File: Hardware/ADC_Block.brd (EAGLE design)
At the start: 30.5 x 44.5 mm, 28 parts, among them U1 ADS1015, U2 PCA9306

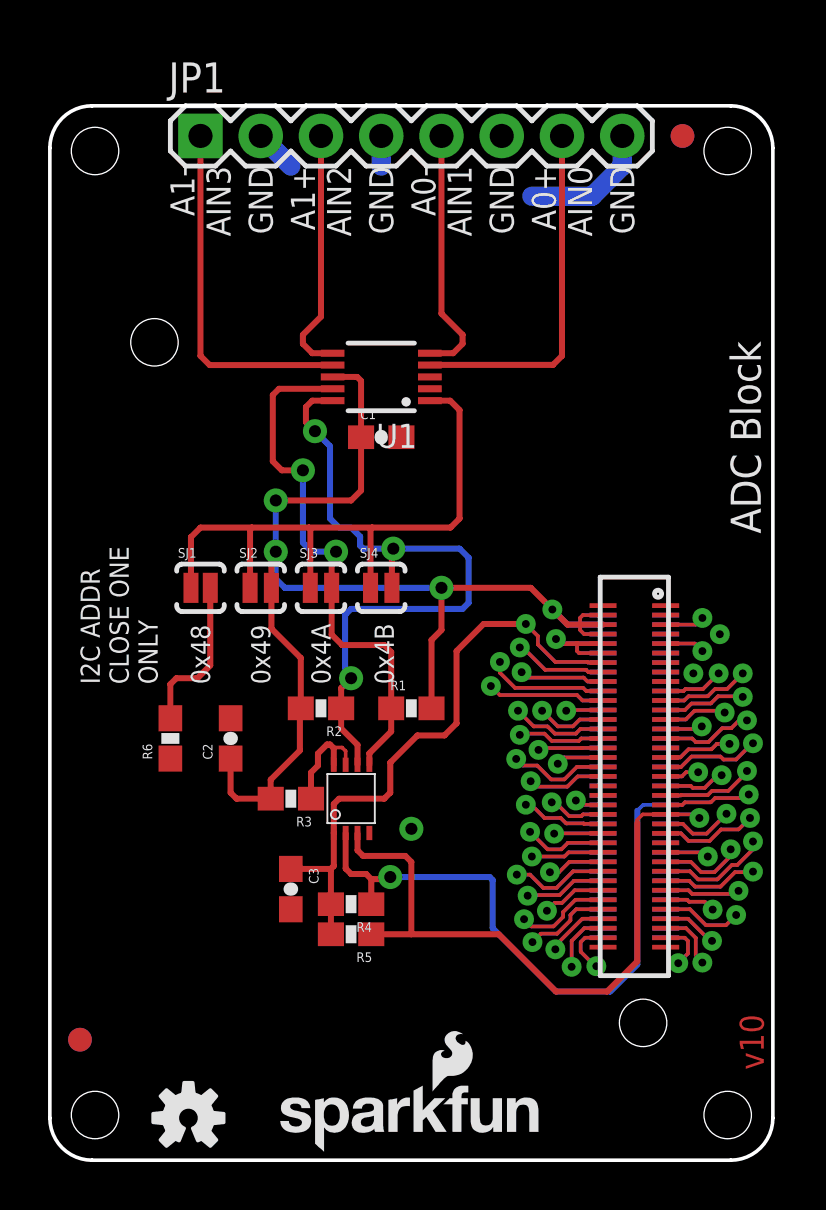
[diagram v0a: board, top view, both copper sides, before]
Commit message: made modifications to add a 3.3v reference voltage and power supply to measure potentiometers from. This will allow the block to be used in a stand alone mode.
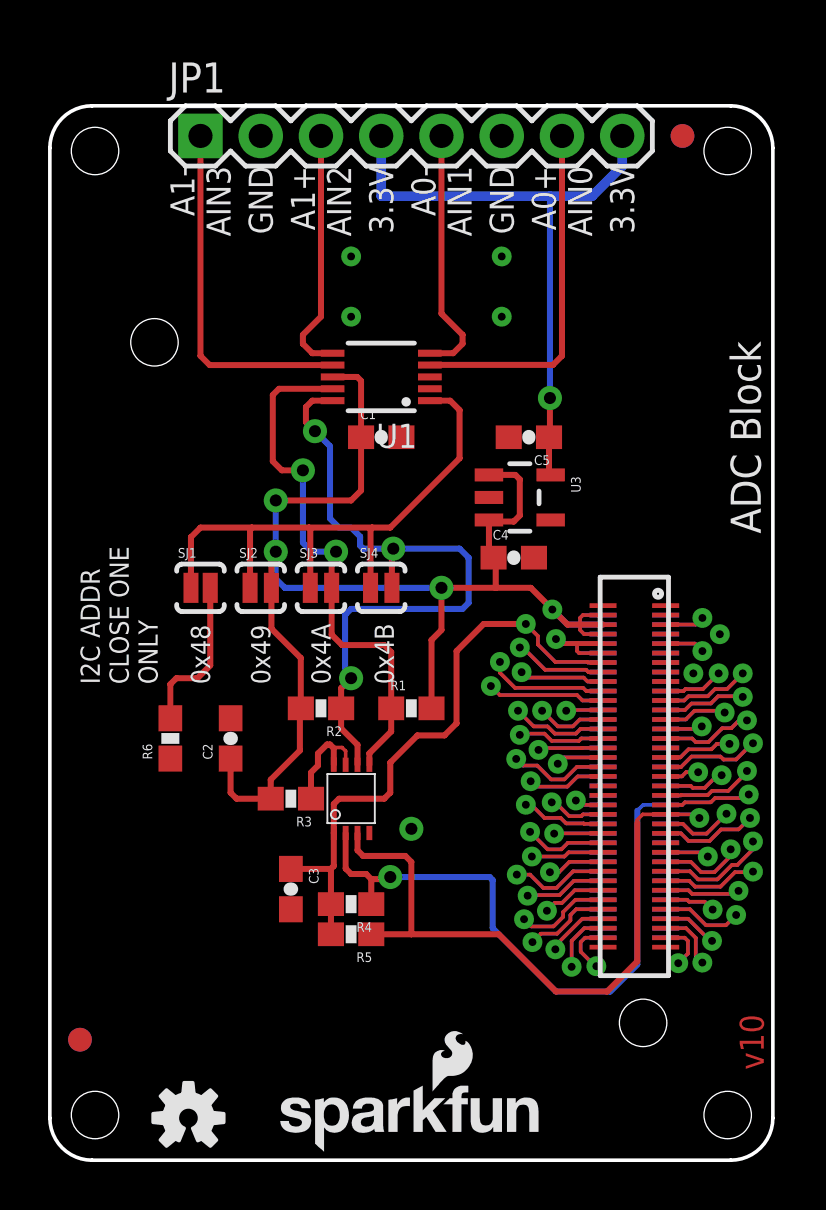
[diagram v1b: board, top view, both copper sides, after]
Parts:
- added C4, C5: 0.1uF, SparkFun-Capacitors:0603-CAP
- added U3: (no value), SparkFun-PowerIC:SOT23-5
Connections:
- new net VREF: C5.1, JP1.4, JP1.8, U3.5
- net GND: now also C4.2, C5.2, U3.2; no longer JP1.4, JP1.8
- net VSYS: now also C4.1, U3.1, U3.3
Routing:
- net VREF: track 0.00 -> 26.3 mm, vias 0 -> 1
- net GND: track 8.67 -> 0.00 mm, vias 3 -> 7
- net VSYS: track 57.3 -> 64.6 mm
- net ADDR: track 27.5 -> 26.0 mm
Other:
- board text added: "3.3V"
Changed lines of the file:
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@@
 <?xml version="1.0" encoding="utf-8"?>
 <!DOCTYPE eagle SYSTEM "eagle.dtd">
-<eagle version="6.6.0">
+<eagle version="6.5.0">
 <drawing>
 <settings>
@@
 <setting verticaltext="up"/>
 </settings>
-<grid distance="0.05" unitdist="inch" unit="inch" style="lines" multiple="1" display="yes" altdistance="0.005" altunitdist="inch" altunit="inch"/>
+<grid distance="0.005" unitdist="inch" unit="inch" style="lines" multiple="1" display="yes" altdistance="0.005" altunitdist="inch" altunit="inch"/>
 <layers>
 <layer number="1" name="Top" color="4" fill="1" visible="yes" active="yes"/>
 <layer number="2" name="Route2" color="1" fill="3" visible="no" active="yes"/>
 <layer number="15" name="Route15" color="4" fill="6" visible="no" active="yes"/>
-<layer number="16" name="Bottom" color="1" fill="1" visible="no" active="yes"/>
+<layer number="16" name="Bottom" color="1" fill="1" visible="yes" active="yes"/>
 <layer number="17" name="Pads" color="2" fill="1" visible="yes" active="yes"/>
 <layer number="18" name="Vias" color="2" fill="1" visible="yes" active="yes"/>
@@
 <layer number="20" name="Dimension" color="15" fill="1" visible="yes" active="yes"/>
 <layer number="21" name="tPlace" color="16" fill="1" visible="yes" active="yes"/>
-<layer number="22" name="bPlace" color="14" fill="1" visible="no" active="yes"/>
+<layer number="22" name="bPlace" color="14" fill="1" visible="yes" active="yes"/>
 <layer number="23" name="tOrigins" color="15" fill="1" visible="yes" active="yes"/>
 <layer number="24" name="bOrigins" color="15" fill="1" visible="no" active="yes"/>
@@
 <text x="30.099" y="3.81" size="1.016" layer="1" font="vector" ratio="15" rot="R90">v10</text>
 <text x="8.89" y="41.91" size="1.016" layer="22" font="vector" ratio="15" rot="SMR270" align="center-left">GND</text>
-<text x="13.97" y="41.91" size="1.016" layer="22" font="vector" ratio="15" rot="SMR270" align="center-left">GND</text>
+<text x="13.97" y="41.91" size="1.016" layer="22" font="vector" ratio="15" rot="SMR270" align="center-left">3.3V</text>
 <text x="19.05" y="41.91" size="1.016" layer="22" font="vector" ratio="15" rot="SMR270" align="center-left">GND</text>
-<text x="24.13" y="41.91" size="1.016" layer="22" font="vector" ratio="15" rot="SMR270" align="center-left">GND</text>
+<text x="24.13" y="41.91" size="1.016" layer="22" font="vector" ratio="15" rot="SMR270" align="center-left">3.3V</text>
 <text x="6.35" y="41.91" size="1.016" layer="21" font="vector" ratio="15" rot="R90" align="center-right">A1-
 AIN3</text>
@@
 <text x="11.43" y="41.91" size="1.016" layer="21" font="vector" ratio="15" rot="R90" align="center-right">A1+
 AIN2</text>
-<text x="13.97" y="41.91" size="1.016" layer="21" font="vector" ratio="15" rot="R90" align="center-right">GND</text>
+<text x="13.97" y="41.91" size="1.016" layer="21" font="vector" ratio="15" rot="R90" align="center-right">3.3V</text>
 <text x="16.51" y="41.91" size="1.016" layer="21" font="vector" ratio="15" rot="R90" align="center-right">A0-
 AIN1</text>
@@
 <text x="21.59" y="41.91" size="1.016" layer="21" font="vector" ratio="15" rot="R90" align="center-right">A0+
 AIN0</text>
-<text x="24.13" y="41.91" size="1.016" layer="21" font="vector" ratio="15" rot="R90" align="center-right">GND</text>
+<text x="24.13" y="41.91" size="1.016" layer="21" font="vector" ratio="15" rot="R90" align="center-right">3.3V</text>
 <text x="29.972" y="26.416" size="1.27" layer="21" font="vector" ratio="15" rot="R90">ADC Block</text>
 <text x="31.75" y="-2.54" size="1.778" layer="51" ratio="15">NOTE: Units are in Inches</text>
@@
 <element name="FID3" library="SparkFun-Aesthetics" package="FIDUCIAL-1X2" value="FIDUCIAL1X2" x="26.67" y="43.18" rot="MR0"/>
 <element name="FID4" library="SparkFun-Aesthetics" package="FIDUCIAL-1X2" value="FIDUCIAL1X2" x="1.27" y="5.08" rot="MR0"/>
+<element name="U3" library="SparkFun-PowerIC" package="SOT23-5" value="" x="19.812" y="27.94" rot="R270">
+<attribute name="PROD_ID" value="VREG-00822" x="19.812" y="27.94" size="1.778" layer="27" rot="R270" display="off"/>
+</element>
+<element name="C4" library="SparkFun-Capacitors" package="0603-CAP" value="0.1uF" x="19.558" y="25.4">
+<attribute name="PROD_ID" value="CAP-00810" x="19.558" y="25.4" size="1.778" layer="27" display="off"/>
+</element>
+<element name="C5" library="SparkFun-Capacitors" package="0603-CAP" value="0.1uF" x="20.193" y="30.48" rot="R180">
+<attribute name="PROD_ID" value="CAP-00810" x="20.193" y="30.48" size="1.778" layer="27" rot="R180" display="off"/>
+</element>
 </elements>
 <signals>
@@
 <contactref element="U2" pad="4"/>
 <contactref element="U1" pad="3"/>
-<contactref element="JP1" pad="8"/>
 <contactref element="JP1" pad="2"/>
-<contactref element="JP1" pad="4"/>
 <contactref element="JP1" pad="6"/>
-<wire x1="8.89" y1="43.18" x2="10.16" y2="41.91" width="0.8128" layer="16"/>
-<wire x1="13.97" y1="43.18" x2="13.97" y2="41.91" width="0.8128" layer="16"/>
 <via x="15.24" y="13.97" extent="1-16" drill="0.508"/>
-<wire x1="24.13" y1="43.18" x2="24.13" y2="41.91" width="0.8128" layer="16"/>
-<wire x1="24.13" y1="41.91" x2="22.86" y2="40.64" width="0.8128" layer="16"/>
-<wire x1="22.86" y1="40.64" x2="20.32" y2="40.64" width="0.8128" layer="16"/>
 <contactref element="R6" pad="1"/>
+<via x="19.05" y="35.56" extent="1-16" drill="0.3302"/>
+<via x="12.7" y="35.56" extent="1-16" drill="0.3302"/>
+<via x="19.05" y="38.1" extent="1-16" drill="0.3302"/>
+<via x="12.7" y="38.1" extent="1-16" drill="0.3302"/>
+<contactref element="C4" pad="2"/>
+<contactref element="U3" pad="2"/>
+<contactref element="C5" pad="2"/>
 </signal>
 <signal name="VSYS">
@@
 <wire x1="9.34" y1="25.469" x2="9.525" y2="25.654" width="0.254" layer="1"/>
 <wire x1="21.8262" y1="22.5798" x2="23.32" y2="22.5798" width="0.254" layer="1"/>
-<wire x1="20.276" y1="24.13" x2="16.51" y2="24.13" width="0.254" layer="1"/>
+<wire x1="20.276" y1="24.13" x2="18.796" y2="24.13" width="0.254" layer="1"/>
+<wire x1="18.796" y1="24.13" x2="16.51" y2="24.13" width="0.254" layer="1"/>
 <wire x1="21.8262" y1="22.5798" x2="21.1904" y2="23.2156" width="0.254" layer="1"/>
 <wire x1="21.1904" y1="23.2156" x2="21.1836" y2="23.2156" width="0.254" layer="1"/>
@@
 <wire x1="23.32" y1="22.5798" x2="22.3782" y2="22.5798" width="0.1524" layer="1"/>
 <wire x1="22.3782" y1="22.5798" x2="22.352" y2="22.606" width="0.1524" layer="1"/>
+<contactref element="U3" pad="3"/>
+<contactref element="U3" pad="1"/>
+<contactref element="C4" pad="1"/>
+<wire x1="18.708" y1="25.4" x2="18.796" y2="25.312" width="0.254" layer="1"/>
+<wire x1="18.796" y1="25.312" x2="18.796" y2="24.13" width="0.254" layer="1"/>
+<wire x1="18.5119" y1="26.99" x2="18.5119" y2="26.924" width="0.254" layer="1"/>
+<wire x1="18.5119" y1="26.924" x2="18.5119" y2="25.5961" width="0.254" layer="1"/>
+<wire x1="18.5119" y1="25.5961" x2="18.708" y2="25.4" width="0.254" layer="1"/>
+<wire x1="18.5119" y1="28.89" x2="19.624" y2="28.89" width="0.254" layer="1"/>
+<wire x1="19.624" y1="28.89" x2="19.812" y2="28.702" width="0.254" layer="1"/>
+<wire x1="19.812" y1="28.702" x2="19.812" y2="27.178" width="0.254" layer="1"/>
+<wire x1="19.812" y1="27.178" x2="19.558" y2="26.924" width="0.254" layer="1"/>
+<wire x1="19.558" y1="26.924" x2="18.5119" y2="26.924" width="0.254" layer="1"/>
 </signal>
 <signal name="3.3V">
@@
 <wire x1="8.509" y1="26.67" x2="10.922" y2="26.67" width="0.254" layer="1"/>
 <wire x1="10.922" y1="26.67" x2="13.589" y2="26.67" width="0.254" layer="1"/>
-<wire x1="13.589" y1="26.67" x2="16.891" y2="26.67" width="0.254" layer="1"/>
-<wire x1="16.891" y1="26.67" x2="17.272" y2="27.051" width="0.254" layer="1"/>
-<wire x1="17.272" y1="27.051" x2="17.272" y2="31.623" width="0.254" layer="1"/>
+<wire x1="13.589" y1="26.67" x2="14.351" y2="26.67" width="0.254" layer="1"/>
+<wire x1="14.351" y1="26.67" x2="17.272" y2="29.591" width="0.254" layer="1"/>
+<wire x1="17.272" y1="29.591" x2="17.272" y2="31.623" width="0.254" layer="1"/>
 <wire x1="16.02" y1="32.02" x2="16.875" y2="32.02" width="0.254" layer="1"/>
 <wire x1="16.875" y1="32.02" x2="17.272" y2="31.623" width="0.254" layer="1"/>
@@
 <wire x1="23.3142" y1="20.574" x2="23.32" y2="20.5798" width="0.1524" layer="1"/>
 </signal>
+<signal name="VREF">
+<contactref element="JP1" pad="4"/>
+<contactref element="JP1" pad="8"/>
+<wire x1="24.13" y1="43.18" x2="24.13" y2="41.91" width="0.4064" layer="16"/>
+<wire x1="24.13" y1="41.91" x2="22.86" y2="40.64" width="0.4064" layer="16"/>
+<wire x1="22.86" y1="40.64" x2="21.082" y2="40.64" width="0.4064" layer="16"/>
+<wire x1="21.082" y1="40.64" x2="13.97" y2="40.64" width="0.4064" layer="16"/>
+<wire x1="13.97" y1="40.64" x2="13.97" y2="43.18" width="0.4064" layer="16"/>
+<contactref element="U3" pad="5"/>
+<contactref element="C5" pad="1"/>
+<wire x1="21.1121" y1="28.89" x2="21.043" y2="28.9591" width="0.254" layer="1"/>
+<wire x1="21.043" y1="28.9591" x2="21.043" y2="30.48" width="0.254" layer="1"/>
+<wire x1="21.043" y1="30.48" x2="21.082" y2="30.519" width="0.254" layer="1"/>
+<wire x1="21.082" y1="30.519" x2="21.082" y2="32.131" width="0.254" layer="1"/>
+<via x="21.082" y="32.131" extent="1-16" drill="0.508"/>
+<wire x1="21.082" y1="32.131" x2="21.082" y2="40.64" width="0.254" layer="16"/>
+</signal>
 </signals>

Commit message: updated rev number
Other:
- board text added: "v20"
- board text removed: "v10"
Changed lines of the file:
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@@
 <rectangle x1="22.098" y1="26.162" x2="30.48" y2="44.45" layer="41" rot="R180"/>
 <text x="29.21" y="6.35" size="1.016" layer="22" font="vector" ratio="15" rot="SMR270" align="center">4xM2.0</text>
-<text x="30.099" y="3.81" size="1.016" layer="1" font="vector" ratio="15" rot="R90">v10</text>
+<text x="30.099" y="3.81" size="1.016" layer="1" font="vector" ratio="15" rot="R90">v20</text>
 <text x="8.89" y="41.91" size="1.016" layer="22" font="vector" ratio="15" rot="SMR270" align="center-left">GND</text>
 <text x="13.97" y="41.91" size="1.016" layer="22" font="vector" ratio="15" rot="SMR270" align="center-left">3.3V</text>

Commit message: added ground vias and removed right angle trace
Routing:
- net VREF: track 26.3 -> 25.6 mm
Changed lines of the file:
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@@
 <contactref element="U3" pad="2"/>
 <contactref element="C5" pad="2"/>
+<via x="15.367" y="38.1" extent="1-16" drill="0.3302"/>
+<via x="15.367" y="35.56" extent="1-16" drill="0.3302"/>
+<via x="9.779" y="35.56" extent="1-16" drill="0.3302"/>
+<via x="9.779" y="38.1" extent="1-16" drill="0.3302"/>
+<via x="7.747" y="38.1" extent="1-16" drill="0.3302"/>
+<via x="7.747" y="35.56" extent="1-16" drill="0.3302"/>
 </signal>
 <signal name="VSYS">
@@
 <wire x1="24.13" y1="41.91" x2="22.86" y2="40.64" width="0.4064" layer="16"/>
 <wire x1="22.86" y1="40.64" x2="21.082" y2="40.64" width="0.4064" layer="16"/>
-<wire x1="21.082" y1="40.64" x2="13.97" y2="40.64" width="0.4064" layer="16"/>
-<wire x1="13.97" y1="40.64" x2="13.97" y2="43.18" width="0.4064" layer="16"/>
 <contactref element="U3" pad="5"/>
 <contactref element="C5" pad="1"/>
@@
 <via x="21.082" y="32.131" extent="1-16" drill="0.508"/>
 <wire x1="21.082" y1="32.131" x2="21.082" y2="40.64" width="0.254" layer="16"/>
+<wire x1="21.082" y1="40.64" x2="15.113" y2="40.64" width="0.4064" layer="16"/>
+<wire x1="15.113" y1="40.64" x2="13.97" y2="41.783" width="0.4064" layer="16"/>
+<wire x1="13.97" y1="41.783" x2="13.97" y2="43.18" width="0.4064" layer="16"/>
 </signal>
 </signals>

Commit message: corrected issues in github
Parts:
- removed U$2: EDISON_CONNECTOR_FULLMOUNTING_HOLES, Edison:EDISON_DAUGHTER
- removed U$3: EDISON_CONNECTOR_FULLHEADER, Edison:DF40C-70DP-0.4(51)
- added JP2: EDISON_CONNECTOR_FULLMOUNTING_HOLES, SparkFun-Boards:EDISON_DAUGHTER
- added JP3: EDISON_CONNECTOR_FULLHEADER, SparkFun-Boards:DF40C-70DP-0.4(51)
- FRAME1, FRAME2: value FRAME-LETTER -> (none)
- JP1: device SparkFun-Connectors:1X08 -> SparkFun-Connectors:1X08_ROUND
- U3: value (none) -> 3.3V
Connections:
- net 1.8V: now also JP2.12, JP3.12; no longer U$2.12, U$3.12
- net 3.3V: now also JP2.10, JP2.8, JP3.10, JP3.8; no longer U$2.10, U$2.8, U$3.10, U$3.8
- net DCIN: now also JP2.14, JP3.14; no longer U$2.14, U$3.14
- net FAULT: now also JP2.19, JP3.19; no longer U$2.19, U$3.19
- net FW_RCVR: now also JP2.69, JP3.69; no longer U$2.69, U$3.69
- net GND: now also JP2.1, JP2.11, JP2.13, JP2.15, JP2.5, JP2.9, JP3.1, JP3.11, JP3.13, JP3.15, JP3.5, JP3.9; no longer U$2.1, U$2.11, U$2.13, U$2.15, U$2.5, U$2.9, U$3.1, U$3.11, U$3.13, U$3.15, U$3.5, U$3.9
- net GP109_SPI_2_CLK: now also JP2.55, JP3.55; no longer U$2.55, U$3.55
- net GP110_SPI_2_FS0: now also JP2.53, JP3.53; no longer U$2.53, U$3.53
- net GP111_SPI_2_FS1: now also JP2.51, JP3.51; no longer U$2.51, U$3.51
- net GP114_SPI_2_RXD: now also JP2.59, JP3.59; no longer U$2.59, U$3.59
- net GP115_SPI_2_TXD: now also JP2.57, JP3.57; no longer U$2.57, U$3.57
- net GP128_UART_1_CTS: now also JP2.65, JP3.65; no longer U$2.65, U$3.65
- net GP129_UART_1_RTS: now also JP2.63, JP3.63; no longer U$2.63, U$3.63
- net GP12_PWM0: now also JP2.35, JP3.35; no longer U$2.35, U$3.35
- net GP130_UART_1_RX: now also JP2.61, JP3.61; no longer U$2.61, U$3.61
- net GP131_UART_1_TX: now also JP2.46, JP3.46; no longer U$2.46, U$3.46
- net GP134_UART_2_RX: now also JP2.22, JP3.22; no longer U$2.22, U$3.22
- net GP135_UART_2_TX: now also JP2.27, JP3.27; no longer U$2.27, U$3.27
- net GP13_PWM1: now also JP2.33, JP3.33; no longer U$2.33, U$3.33
- net GP14: now also JP2.48, JP3.48; no longer U$2.48, U$3.48
- net GP15: now also JP2.42, JP3.42; no longer U$2.42, U$3.42
- net GP165: now also JP2.25, JP3.25; no longer U$2.25, U$3.25
- net GP182_PWM2: now also JP2.37, JP3.37; no longer U$2.37, U$3.37
- net GP183_PWM3: now also JP2.39, JP3.39; no longer U$2.39, U$3.39
- net GP19_I2C_1_SCL: now also JP2.41, JP3.41; no longer U$2.41, U$3.41
- net GP20_I2C_1_SDA: now also JP2.43, JP3.43; no longer U$2.43, U$3.43
- net GP27_I2C_6_SCL: now also JP2.45, JP3.45; no longer U$2.45, U$3.45
- net GP28_I2C_6_SDA: now also JP2.47, JP3.47; no longer U$2.47, U$3.47
- net GP40_I2S_2_CLK: now also JP2.52, JP3.52; no longer U$2.52, U$3.52
- net GP41_I2S_2_FS: now also JP2.54, JP3.54; no longer U$2.54, U$3.54
- net GP42_I2S_2_RXD: now also JP2.50, JP3.50; no longer U$2.50, U$3.50
- net GP43_I2S_2_TXD: now also JP2.56, JP3.56; no longer U$2.56, U$3.56
- net GP44: now also JP2.24, JP3.24; no longer U$2.24, U$3.24
- net GP45: now also JP2.26, JP3.26; no longer U$2.26, U$3.26
- net GP46: now also JP2.28, JP3.28; no longer U$2.28, U$3.28
- net GP47: now also JP2.30, JP3.30; no longer U$2.30, U$3.30
- net GP48: now also JP2.32, JP3.32; no longer U$2.32, U$3.32
- net GP49: now also JP2.34, JP3.34; no longer U$2.34, U$3.34
- net GP77_SD_0_CD#: now also JP2.60, JP3.60; no longer U$2.60, U$3.60
- net GP78_SD_0_CLK: now also JP2.58, JP3.58; no longer U$2.58, U$3.58
- net GP79_SD_0_CMD: now also JP2.62, JP3.62; no longer U$2.62, U$3.62
- net GP80_SD_0_DAT0: now also JP2.66, JP3.66; no longer U$2.66, U$3.66
- net GP81_SD_0_DAT1: now also JP2.70, JP3.70; no longer U$2.70, U$3.70
- net GP82_SD_0_DAT2: now also JP2.64, JP3.64; no longer U$2.64, U$3.64
- net GP83_SD_0_DAT3: now also JP2.68, JP3.68; no longer U$2.68, U$3.68
- net GP84_SD_CLK_FB: now also JP2.44, JP3.44; no longer U$2.44, U$3.44
- net MSIC_SLP_CLK: now also JP2.7, JP3.7; no longer U$2.7, U$3.7
- net OSC_CLK_OUT: now also JP2.67, JP3.67; no longer U$2.67, U$3.67
- net PSW: now also JP2.21, JP3.21; no longer U$2.21, U$3.21
- net PWRBTN#: now also JP2.17, JP3.17; no longer U$2.17, U$3.17
- net RCVR_MODE: now also JP2.31, JP3.31; no longer U$2.31, U$3.31
- net RESET_OUT#: now also JP2.36, JP3.36; no longer U$2.36, U$3.36
- net USB_DN: now also JP2.18, JP3.18; no longer U$2.18, U$3.18
- net USB_DP: now also JP2.16, JP3.16; no longer U$2.16, U$3.16
- net USB_ID: now also JP2.3, JP3.3; no longer U$2.3, U$3.3
- net USB_VBUS: now also JP2.20, JP3.20; no longer U$2.20, U$3.20
- net VSYS: now also JP2.2, JP2.4, JP2.6, JP3.2, JP3.4, JP3.6; no longer U$2.2, U$2.4, U$2.6, U$3.2, U$3.4, U$3.6
- net V_BAT_BKUP: now also JP2.23, JP3.23; no longer U$2.23, U$3.23
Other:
- board text added: "Revised 3/15 - Casey Kuhns"
